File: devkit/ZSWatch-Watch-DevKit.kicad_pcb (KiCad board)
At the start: 4 copper layers, 100 x 70 mm, 130 parts, among them IC401 nPM1300-QEXX, IC501 APDS-9306-065, IC502 BMI270, IC503 LIS2MDLTR, IC504 BMP581, IC505 DRV2603RUNT, IC506 PCA9306JK, IC507 RV-8263-C8, IC601 FAN5622SX, IC602 USBLC6-2P6, IC603 MX25U51245GZ4I00, IC604 NTS0104GU12, M601 NORA-B106, Q401 PMZ550UNEYL, Q402 PMZ550UNEYL, Q403 PMZ550UNEYL, Q404 PMZB320UPEYL, X401 Battery, X402 Battery, X403 Power, X404 VSYS, X501 Current, X502 I2S, X503 Current, X504 I2C, X505 Current, X506 Current, X507 Current, X508 Current, X509 Motor, X510 Current, X601 DEBUG, X602 Current, X603 Device, X604 UART, X605 GPIO, X606 Current, X607 IO Current, X608 Display, X609 Current, X610 LED Current

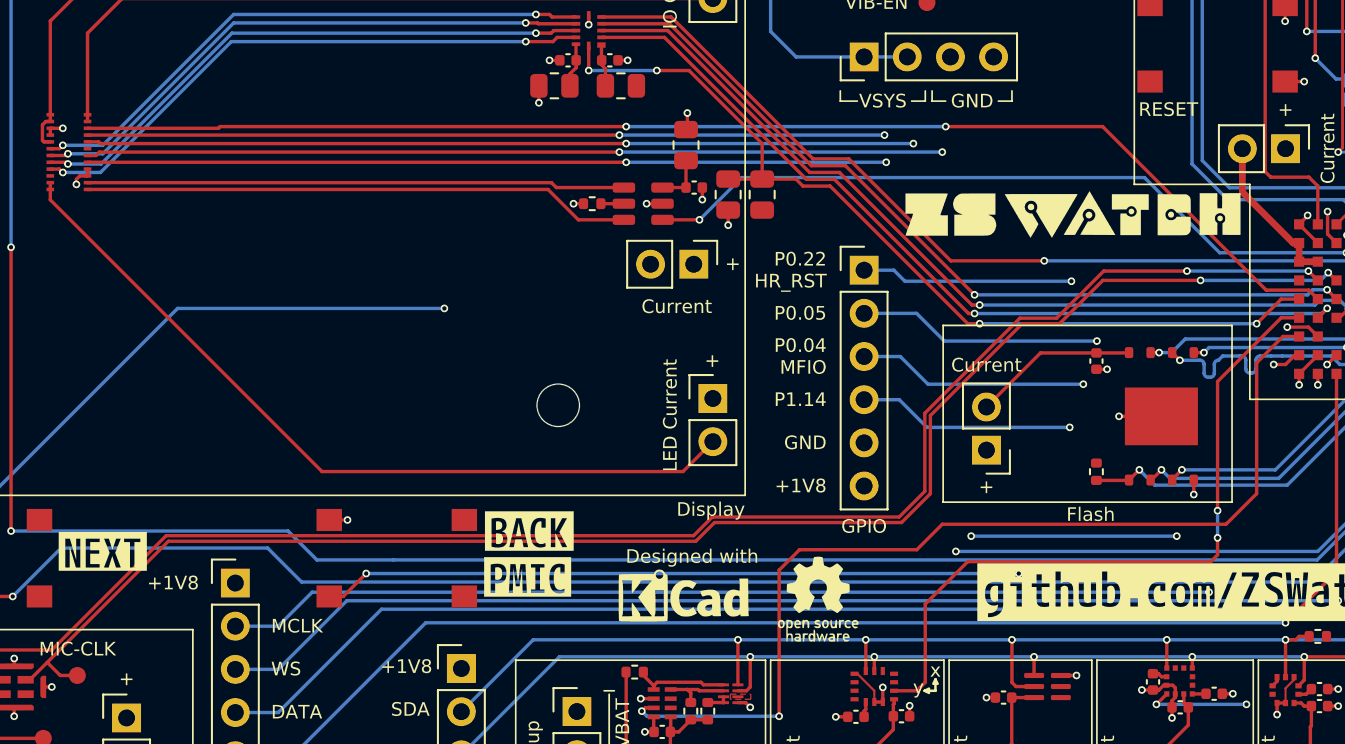
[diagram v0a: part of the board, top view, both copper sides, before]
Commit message: Add logo and QR code to backside silkscreen.
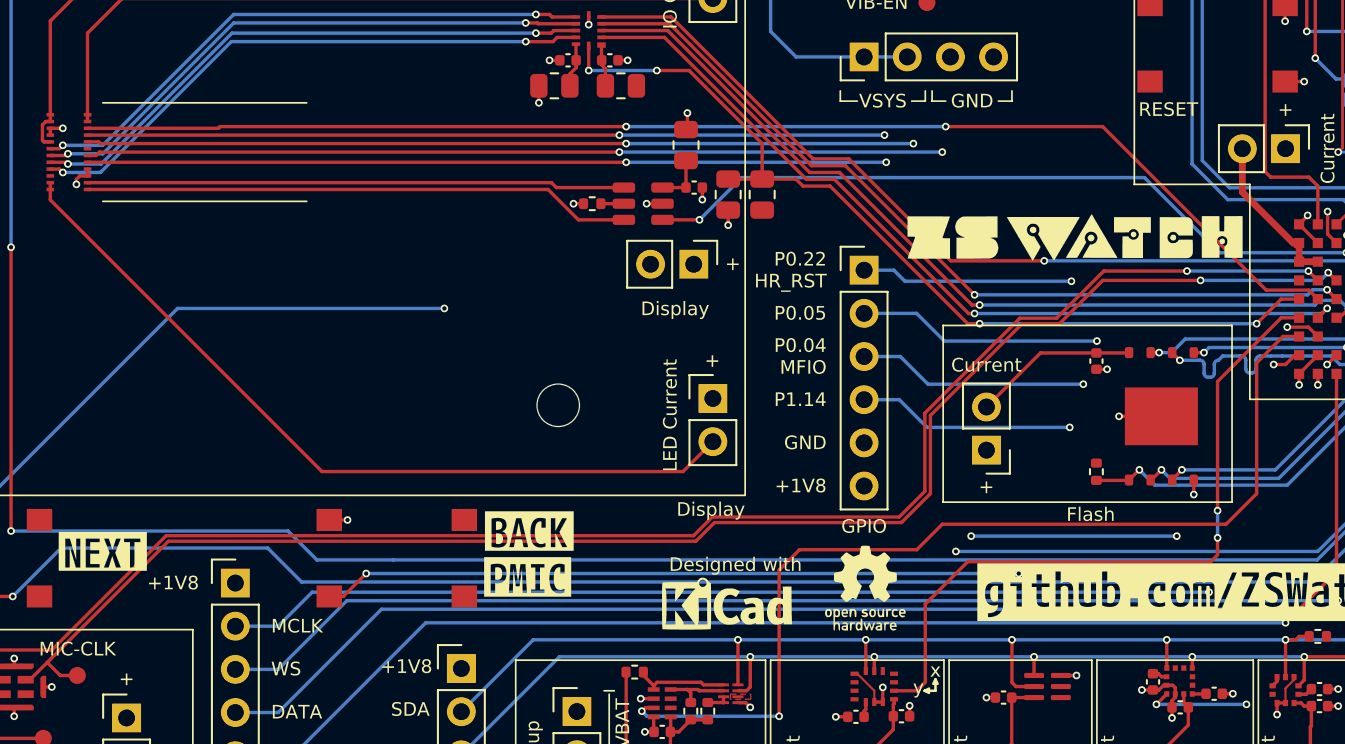
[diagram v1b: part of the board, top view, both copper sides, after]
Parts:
- added G***: LOGO, LOGO, B.Cu at (184.2, 142.4)
- added G***: LOGO, LOGO, B.Cu at (174.6, 127.2)
- X609: value Current -> Display
- moved G*** 2.85 mm to (218.6, 167.8)
- moved G*** 2.59 mm to (210.6, 168.6)
- moved G*** 1.36 mm to (230.8, 147.1)

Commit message: Revert "Add logo and QR code to backside silkscreen."
This reverts commit 72bffc7b9b4678faa50e0150c8a60641f706a446.
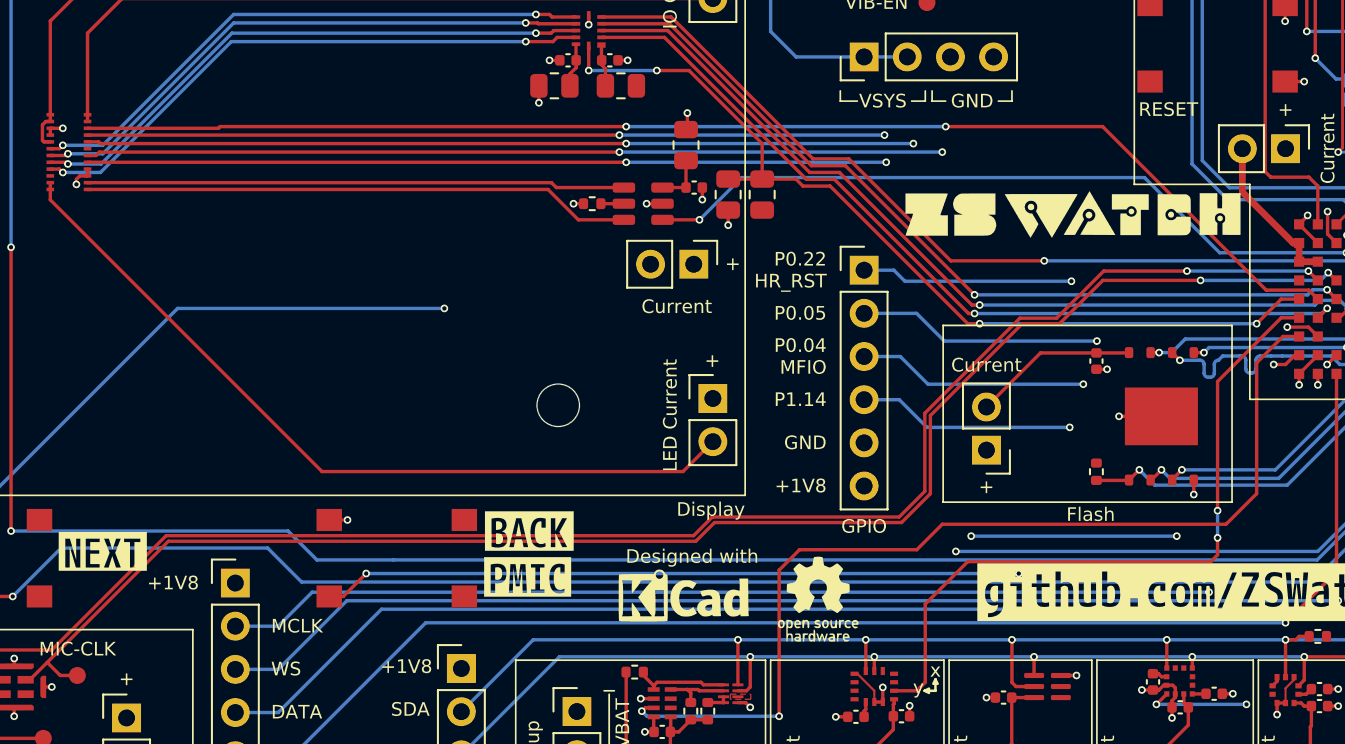
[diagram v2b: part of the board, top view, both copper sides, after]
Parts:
- removed the G*** at (184.2, 142.4)
- removed the G*** at (174.6, 127.2)
- X609: value Display -> Current
- moved G*** 2.85 mm to (215.8, 168.4)
- moved G*** 2.59 mm to (208.0, 168.1)
- moved G*** 1.36 mm to (230.7, 145.7)

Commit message: Revert "Feature: Issue #186"
This reverts commit 73512b60dac517a3d61ff56758c38d705b52f64d.
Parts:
- X510: footprint Connector_PinHeader_2.54mm:PinHeader_1x03_P2.54mm_Vertical -> Connector_PinHeader_2.54mm:PinHeader_1x02_P2.54mm_Vertical
- moved R505 2.89 mm to (207.9, 172.6)
- moved X510 2.75 mm to (203.2, 177.3)
- moved R503 1.12 mm to (210.4, 175.2), turned to 0 degrees
- moved IC506 0.35 mm to (210.3, 174.0)
- moved R504 0.20 mm to (208.3, 175.2)
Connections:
- R503 pad 1: Net-(IC507-V_{DD}) -> Net-(IC506-EN)
- R503 pad 2: Net-(IC506-EN) -> /Project Architecture/Peripherals/VBAT
- R504 pad 2: Net-(IC507-V_{DD}) -> /Project Architecture/Peripherals/VBAT
- R505 pad 2: Net-(IC507-V_{DD}) -> /Project Architecture/Peripherals/VBAT
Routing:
- net /Project Architecture/Power Management/VSYS: track 274.0 -> 224.2 mm
- net Net-(IC507-V_{DD}): track 15.2 -> 8.13 mm
- net /Project Architecture/Peripherals/VBAT: track 22.1 -> 24.0 mm, vias 2 -> 5
- net Net-(IC506-SDA_{2}): track 5.53 -> 4.91 mm
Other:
- board text removed: "Backup"
- board text removed: "VBAT"

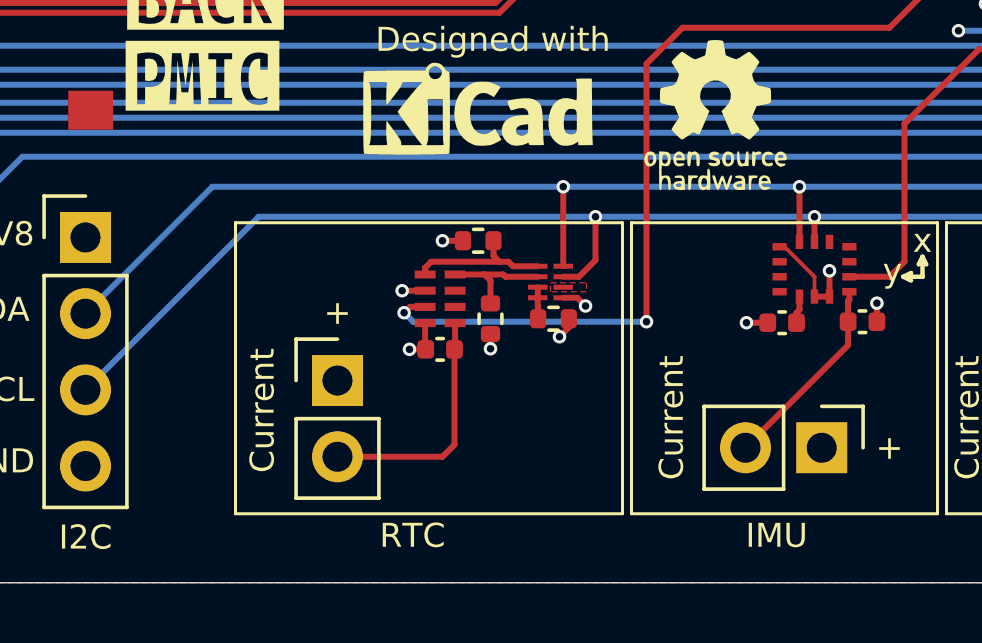
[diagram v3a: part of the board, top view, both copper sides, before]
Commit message: Feature: Issue #186
Allow powering RTC from any voltage source

Closes #186

Signed-off-by: Daniel Kampert <DanielKampert@kampis-elektroecke.de>
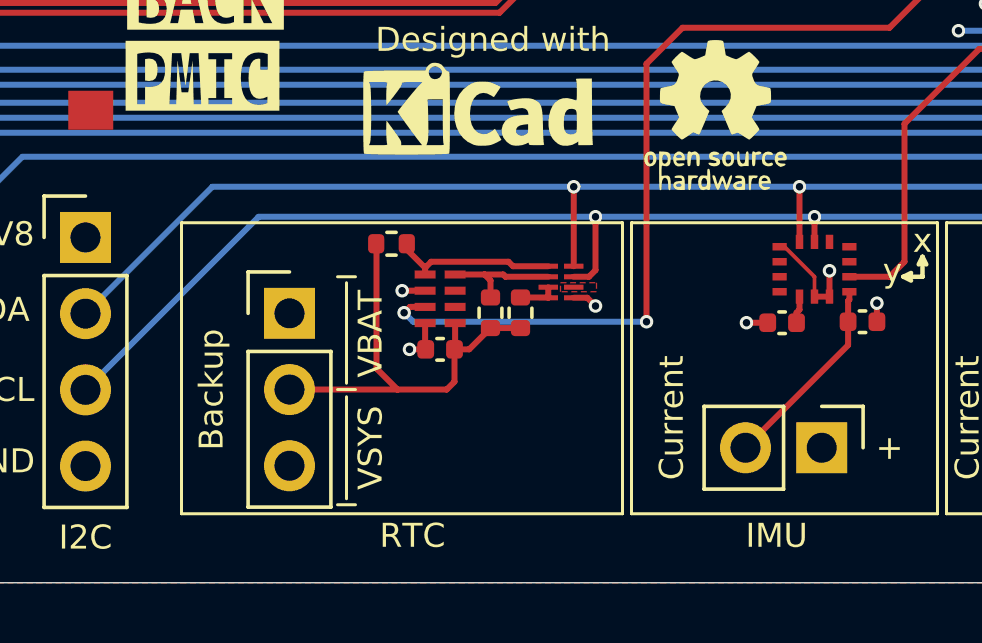
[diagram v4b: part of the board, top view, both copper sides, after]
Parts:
- X510: footprint Connector_PinHeader_2.54mm:PinHeader_1x02_P2.54mm_Vertical -> Connector_PinHeader_2.54mm:PinHeader_1x03_P2.54mm_Vertical
- moved R505 2.89 mm to (205.0, 172.7)
- moved X510 2.75 mm to (201.6, 175.0)
- moved R503 1.12 mm to (209.3, 175.0), turned to 90 degrees
- moved IC506 0.35 mm to (210.7, 174.0)
- moved R504 0.20 mm to (208.3, 175.0)
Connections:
- R503 pad 1: Net-(IC506-EN) -> Net-(IC507-V_{DD})
- R503 pad 2: /Project Architecture/Peripherals/VBAT -> Net-(IC506-EN)
- R504 pad 2: /Project Architecture/Peripherals/VBAT -> Net-(IC507-V_{DD})
- R505 pad 2: /Project Architecture/Peripherals/VBAT -> Net-(IC507-V_{DD})
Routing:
- net /Project Architecture/Power Management/VSYS: track 224.2 -> 274.0 mm
- net Net-(IC507-V_{DD}): track 8.13 -> 15.2 mm
- net /Project Architecture/Peripherals/VBAT: track 24.0 -> 22.1 mm, vias 5 -> 2
- net Net-(IC506-SDA_{2}): track 4.91 -> 5.53 mm
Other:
- board text added: "Backup"
- board text added: "VBAT"
